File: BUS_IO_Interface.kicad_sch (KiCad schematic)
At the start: 28 parts, among them U12 MAX31331TETB+, U13 AS1016204-0108X0PWAY, U14 TCAN1044ADDFRQ1, U16 AS1016204-0108X0PWAY, U18 AS1016204-0108X0PWAY, U20 AS1016204-0108X0PWAY, Y3 32.768kHz

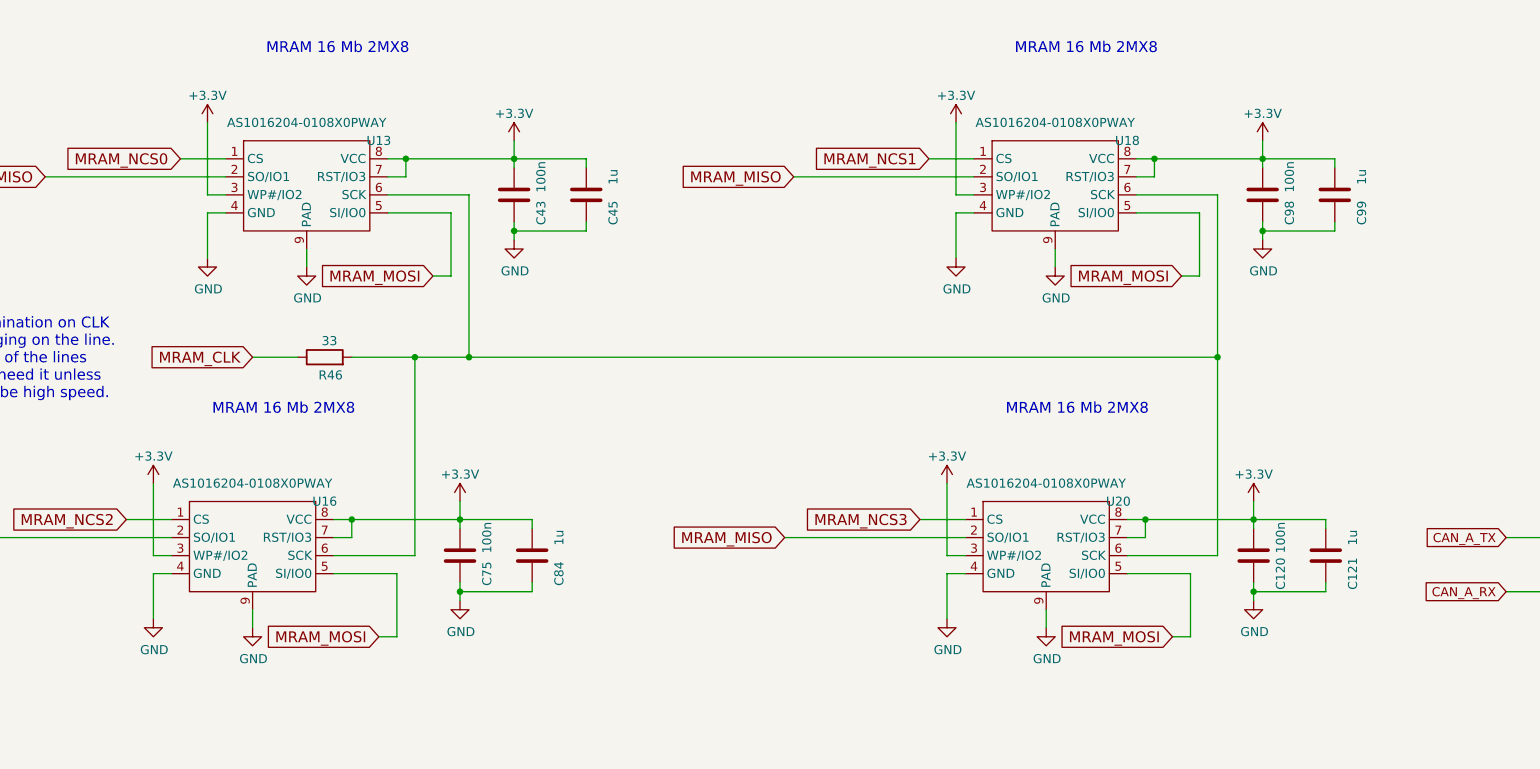
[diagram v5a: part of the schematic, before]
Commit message: Rework the MRAM device interface
Use pull ups instead of connecting pins right to +3.3V.

Signed-off-by: Corey Minyard <corey@minyard.net>
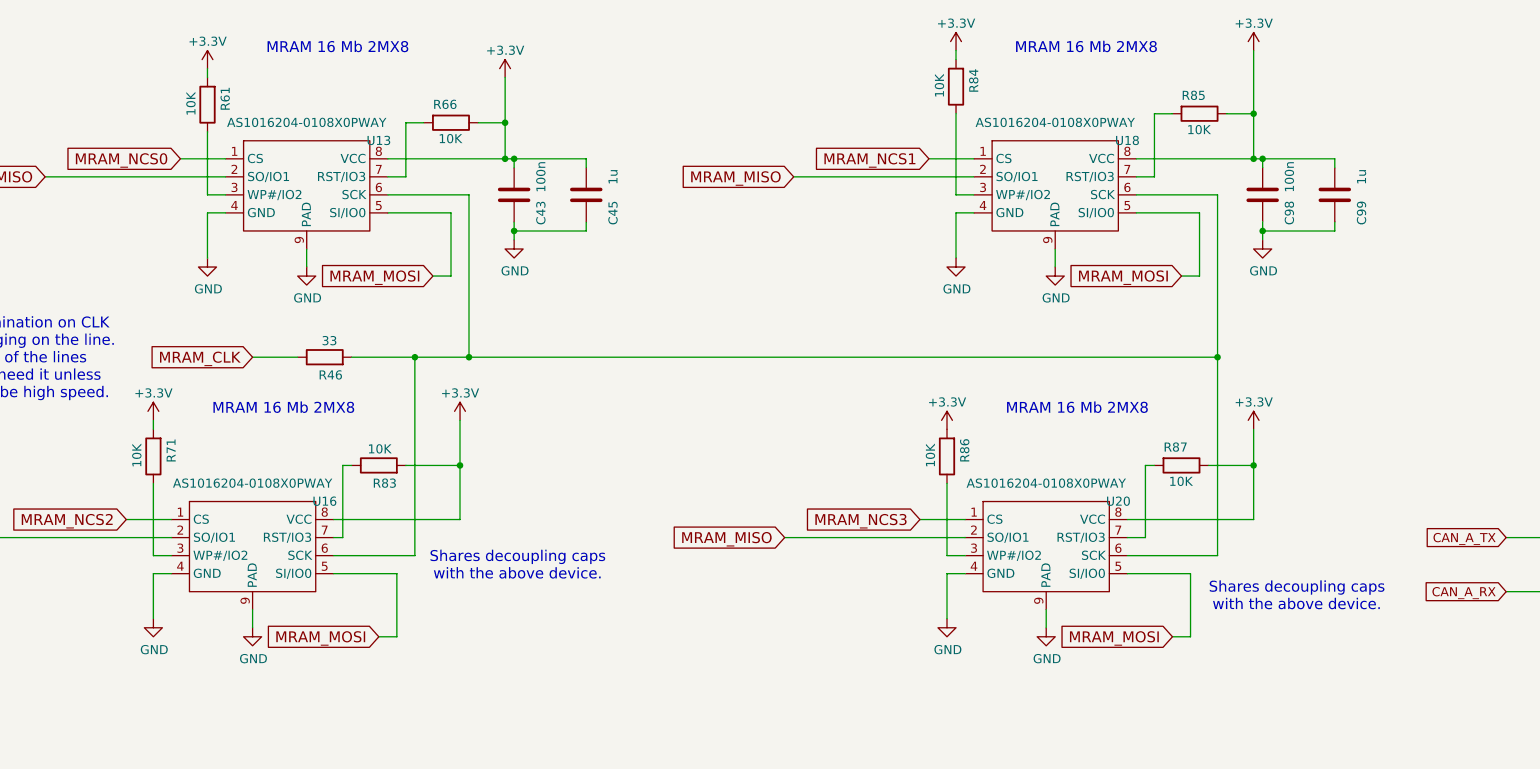
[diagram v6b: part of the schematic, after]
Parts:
- removed C120, C75: 100n, Capacitor_SMD:C_0603_1608Metric_Pad1.08x0.95mm_HandSolder, symbol Device:C
- removed C121, C84: 1u, Capacitor_SMD:C_0603_1608Metric_Pad1.08x0.95mm_HandSolder, symbol Device:C
- added R61, R66, R71, R83, R84, R85, R86, R87: 10K, Resistor_SMD:R_0603_1608Metric_Pad0.98x0.95mm_HandSolder, symbol Device:R
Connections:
- net +3.3V: now also R61.2, R66.1, R71.2, R83.2, R84.2, R85.1, R86.2, R87.1; no longer U13.3 (WP#/IO2), U13.7 (RST/IO3), U16.3 (WP#/IO2), U16.7 (RST/IO3), U18.3 (WP#/IO2), U18.7 (RST/IO3), U20.3 (WP#/IO2), U20.7 (RST/IO3)
- new net: R71.1, U16.3 (WP#/IO2)
- new net: R66.2, U13.7 (RST/IO3)
- new net: R83.1, U16.7 (RST/IO3)
- new net: R84.1, U18.3 (WP#/IO2)
- new net: R85.2, U18.7 (RST/IO3)
- new net: R86.1, U20.3 (WP#/IO2)
- new net: R61.1, U13.3 (WP#/IO2)
- new net: R87.2, U20.7 (RST/IO3)
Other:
- note added: "Shares decoupling caps with the above device."

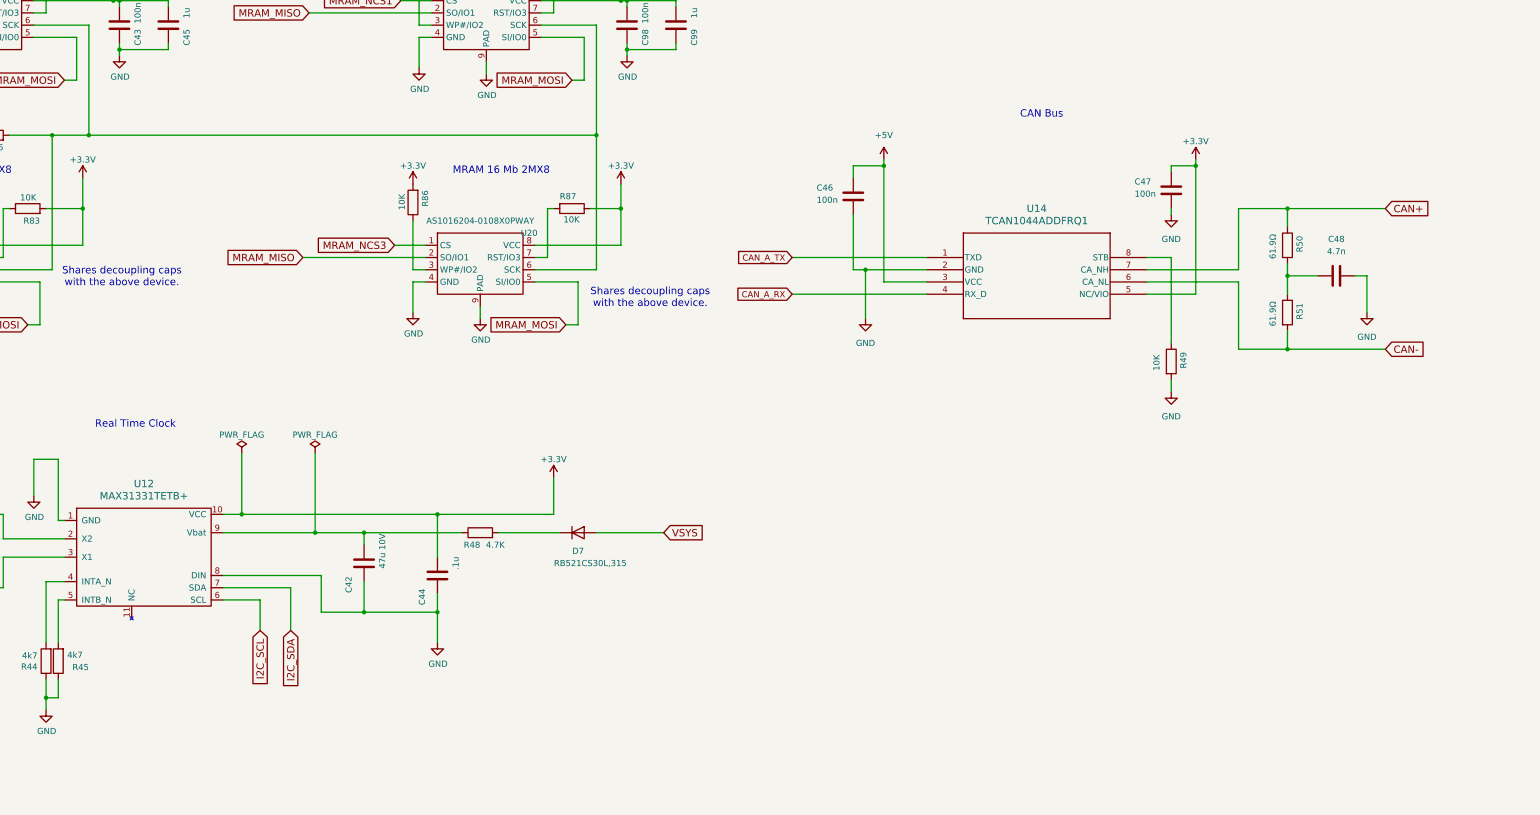
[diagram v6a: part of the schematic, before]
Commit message: Add a second CAN bus interface
Redundancy...

Signed-off-by: Corey Minyard <corey@minyard.net>
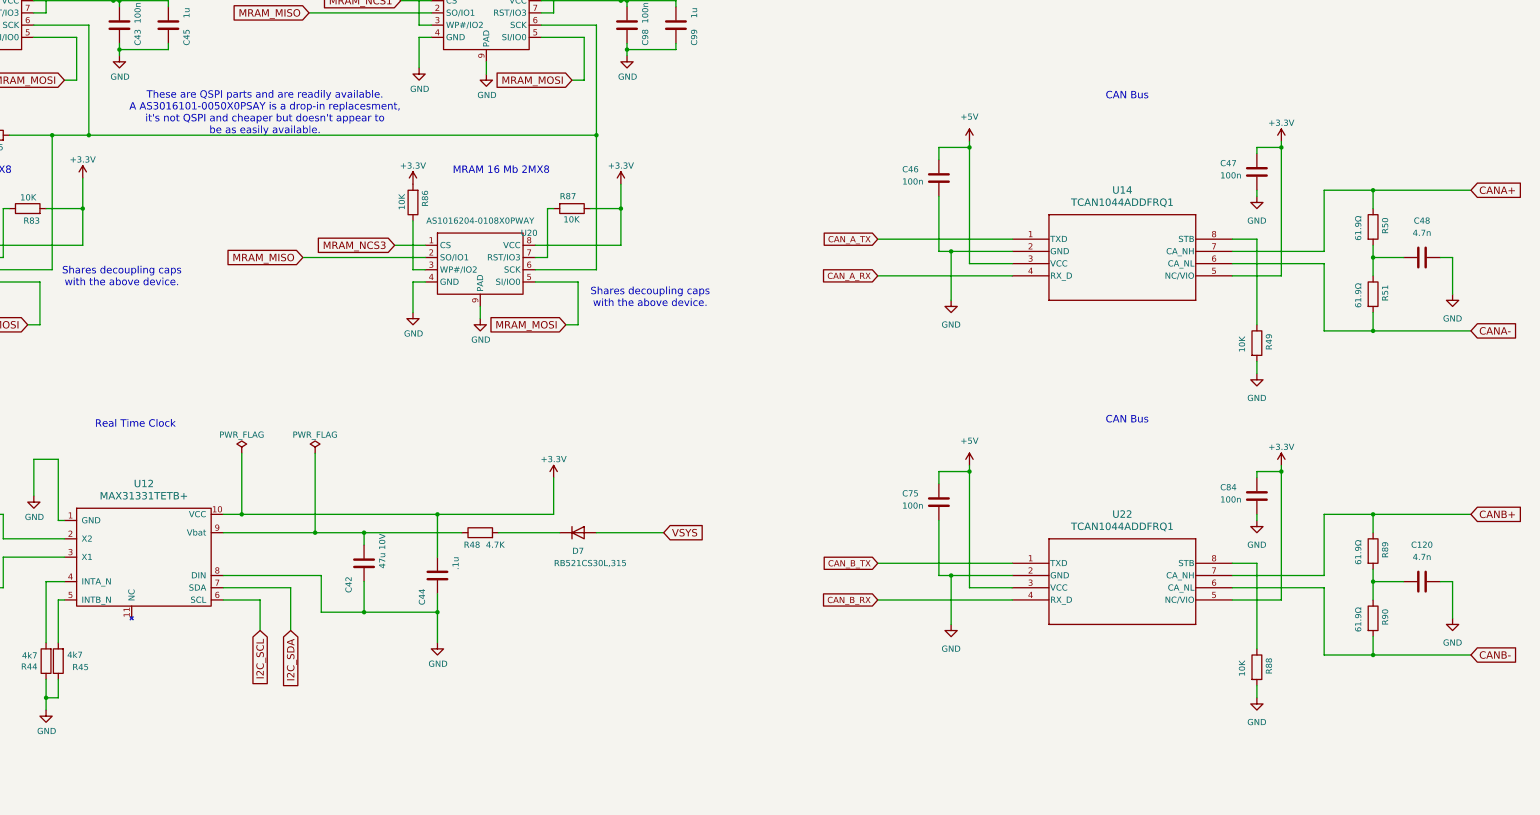
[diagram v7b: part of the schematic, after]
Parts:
- added C120: 4.7n, Capacitor_SMD:C_0603_1608Metric_Pad1.08x0.95mm_HandSolder, symbol Device:C
- added C75, C84: 100n, Capacitor_SMD:C_0603_1608Metric_Pad1.08x0.95mm_HandSolder, symbol Device:C
- added R88: 10K, Resistor_SMD:R_0603_1608Metric_Pad0.98x0.95mm_HandSolder, symbol Device:R
- added R89, R90: 61.9Ω, Resistor_SMD:R_0603_1608Metric_Pad0.98x0.95mm_HandSolder, symbol Device:R
- added U22: TCAN1044ADDFRQ1, Package_TO_SOT_SMD:TSOT-23-8, symbol PACSAT_ICs:TCAN1044ADDFRQ1
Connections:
- net +3.3V: now also C84.1, U22.5 (NC/VIO)
- net +5V: now also C75.1, U22.3 (VCC)
- net GND: now also C120.2, C75.2, C84.2, R88.2, U22.2 (GND)
- net CAN+ renamed CANA+
- net CAN- renamed CANA-
- new net: C120.1, R89.2, R90.1
- new net: R88.1, U22.8 (STB)
- new net CANB+: R89.1, U22.7 (CA_NH)
- new net CANB-: R90.2, U22.6 (CA_NL)
- new net CAN_B_RX: U22.4 (RX_D)
- new net CAN_B_TX: U22.1 (TXD)
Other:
- note added: "These are QSPI parts and are readily available. A AS3016101-0050X0PSAY is a drop-in replacesment, it's not QSPI and cheaper but doesn't appear to be as easily available."
- moved on the sheet: C46, C47, C48, R49, R50, R51, U14

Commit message: Convert a lot of parts to 0402
The passives across the top where things are crowded.

Signed-off-by: Corey Minyard <corey@minyard.net>
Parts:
- C120, C44, C46, C47, C48, C75, C84: footprint Capacitor_SMD:C_0603_1608Metric_Pad1.08x0.95mm_HandSolder -> Capacitor_SMD:C_0402_1005Metric_Pad0.74x0.62mm_HandSolder
- R44, R45, R48, R49, R50, R51, R88, R89, R90: footprint Resistor_SMD:R_0603_1608Metric_Pad0.98x0.95mm_HandSolder -> Resistor_SMD:R_0402_1005Metric_Pad0.72x0.64mm_HandSolder
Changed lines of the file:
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@@
 			)
 		)
-		(property "Footprint" "Resistor_SMD:R_0603_1608Metric_Pad0.98x0.95mm_HandSolder"
+		(property "Footprint" "Resistor_SMD:R_0402_1005Metric_Pad0.72x0.64mm_HandSolder"
 			(at 91.948 176.53 90)
 			(effects
@@
 			)
 		)
-		(property "Footprint" "Resistor_SMD:R_0603_1608Metric_Pad0.98x0.95mm_HandSolder"
+		(property "Footprint" "Resistor_SMD:R_0402_1005Metric_Pad0.72x0.64mm_HandSolder"
 			(at 363.982 167.64 90)
 			(effects
@@
 			)
 		)
-		(property "Footprint" "Resistor_SMD:R_0603_1608Metric_Pad0.98x0.95mm_HandSolder"
+		(property "Footprint" "Resistor_SMD:R_0402_1005Metric_Pad0.72x0.64mm_HandSolder"
 			(at 363.982 100.33 90)
 			(effects
@@
 			)
 		)
-		(property "Footprint" "Capacitor_SMD:C_0603_1608Metric_Pad1.08x0.95mm_HandSolder"
+		(property "Footprint" "Capacitor_SMD:C_0402_1005Metric_Pad0.74x0.62mm_HandSolder"
 			(at 276.5552 80.01 0)
 			(effects
@@
 			)
 		)
-		(property "Footprint" "Capacitor_SMD:C_0603_1608Metric_Pad1.08x0.95mm_HandSolder"
+		(property "Footprint" "Capacitor_SMD:C_0402_1005Metric_Pad0.74x0.62mm_HandSolder"
 			(at 342.5952 78.74 0)
 			(effects
@@
 			)
 		)
-		(property "Footprint" "Capacitor_SMD:C_0603_1608Metric_Pad1.08x0.95mm_HandSolder"
+		(property "Footprint" "Capacitor_SMD:C_0402_1005Metric_Pad0.74x0.62mm_HandSolder"
 			(at 276.5552 147.32 0)
 			(effects
@@
 			)
 		)
-		(property "Footprint" "Capacitor_SMD:C_0603_1608Metric_Pad1.08x0.95mm_HandSolder"
+		(property "Footprint" "Capacitor_SMD:C_0402_1005Metric_Pad0.74x0.62mm_HandSolder"
 			(at 379.73 91.7448 0)
 			(effects
@@
 			)
 		)
-		(property "Footprint" "Capacitor_SMD:C_0603_1608Metric_Pad1.08x0.95mm_HandSolder"
+		(property "Footprint" "Capacitor_SMD:C_0402_1005Metric_Pad0.74x0.62mm_HandSolder"
 			(at 379.73 159.0548 0)
 			(effects
@@
 			)
 		)
-		(property "Footprint" "Resistor_SMD:R_0603_1608Metric_Pad0.98x0.95mm_HandSolder"
+		(property "Footprint" "Resistor_SMD:R_0402_1005Metric_Pad0.72x0.64mm_HandSolder"
 			(at 363.982 86.36 90)
 			(effects
@@
 			)
 		)
-		(property "Footprint" "Capacitor_SMD:C_0603_1608Metric_Pad1.08x0.95mm_HandSolder"
+		(property "Footprint" "Capacitor_SMD:C_0402_1005Metric_Pad0.74x0.62mm_HandSolder"
 			(at 172.4152 162.56 0)
 			(effects
@@
 			)
 		)
-		(property "Footprint" "Resistor_SMD:R_0603_1608Metric_Pad0.98x0.95mm_HandSolder"
+		(property "Footprint" "Resistor_SMD:R_0402_1005Metric_Pad0.72x0.64mm_HandSolder"
 			(at 363.982 153.67 90)
 			(effects
@@
 			)
 		)
-		(property "Footprint" "Resistor_SMD:R_0603_1608Metric_Pad0.98x0.95mm_HandSolder"
+		(property "Footprint" "Resistor_SMD:R_0402_1005Metric_Pad0.72x0.64mm_HandSolder"
 			(at 180.34 151.638 90)
 			(effects
@@
 			)
 		)
-		(property "Footprint" "Resistor_SMD:R_0603_1608Metric_Pad0.98x0.95mm_HandSolder"
+		(property "Footprint" "Resistor_SMD:R_0402_1005Metric_Pad0.72x0.64mm_HandSolder"
 			(at 94.488 176.53 90)
 			(effects
@@
 			)
 		)
-		(property "Footprint" "Resistor_SMD:R_0603_1608Metric_Pad0.98x0.95mm_HandSolder"
+		(property "Footprint" "Resistor_SMD:R_0402_1005Metric_Pad0.72x0.64mm_HandSolder"
 			(at 339.852 177.8 90)
 			(effects
@@
 			)
 		)
-		(property "Footprint" "Resistor_SMD:R_0603_1608Metric_Pad0.98x0.95mm_HandSolder"
+		(property "Footprint" "Resistor_SMD:R_0402_1005Metric_Pad0.72x0.64mm_HandSolder"
 			(at 339.852 110.49 90)
 			(effects
@@
 			)
 		)
-		(property "Footprint" "Capacitor_SMD:C_0603_1608Metric_Pad1.08x0.95mm_HandSolder"
+		(property "Footprint" "Capacitor_SMD:C_0402_1005Metric_Pad0.74x0.62mm_HandSolder"
 			(at 342.5952 146.05 0)
 			(effects
